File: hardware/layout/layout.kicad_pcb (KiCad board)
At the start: 4 copper layers, 50 x 20 mm, 73 parts, among them J1 208658-1001, J2 USB4105-GF-A-060, Q1 2N7002, SW1 TS-1088-AR02016, U1 PCA9306DCTR, U2 AP2112K-3.3TRG1, U3 USBLC6-2SC6, U4 W25Q16JVSSIQ, U5 RP2040, Y1 X322512MSB4SI

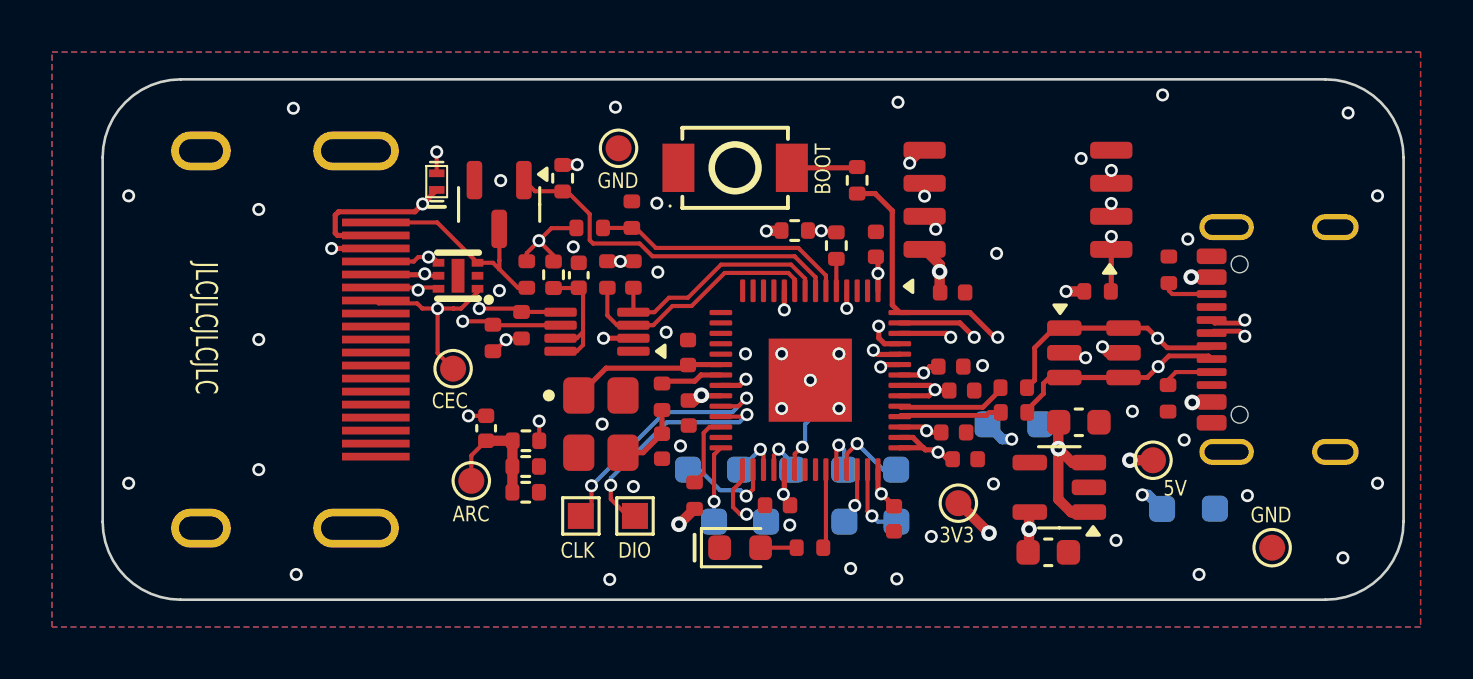
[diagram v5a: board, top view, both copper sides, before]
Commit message: hardware: adjust layout, add jlcpcb export to gitignore
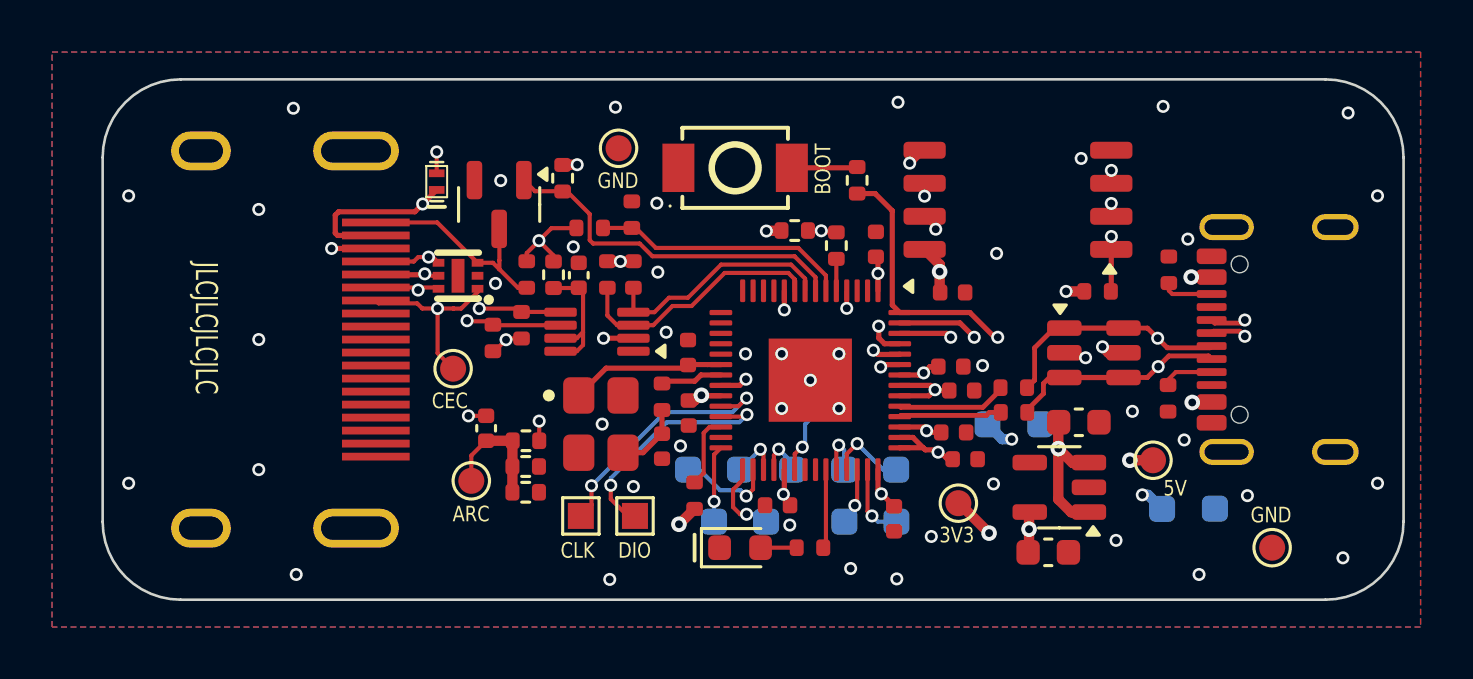
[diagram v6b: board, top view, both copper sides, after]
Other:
- board text added: "gh:naorunaoru/picoarc"
- board text removed: "@naorunaoru"
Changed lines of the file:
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@@
 		)
 	)
-	(gr_text "@naorunaoru"
+	(gr_text "gh:naorunaoru/picoarc"
 		(at 132.58 108.19 0)
 		(layer "B.SilkS")
 		(effects
 			(font
-				(size 1 1)
+				(size 0.8 0.8)
 				(thickness 0.1)
 			)
@@
 	)
 	(via
-		(at 115.25 109.12)
+		(at 115.099171 108.842136)
 		(size 0.5)
 		(drill 0.3)
@@
 	)
 	(via
-		(at 140.74 101.6)
+		(at 140.76 102.04)
 		(size 0.5)
 		(drill 0.3)
@@
 	)
 	(segment
-		(start 113.84 110.3)
+		(start 114.029579 110.3)
 		(end 114.87 110.3)
 		(width 0.16)
@@
 	)
 	(segment
+		(start 114.87 110.3)
+		(end 115 110.43)
+		(width 0.16)
+		(layer "F.Cu")
+		(net "DDC_SCL_5V")
+	)
+	(segment
 		(start 112.380736 108.474819)
 		(end 112.25367 108.474819)
@@
 	)
 	(segment
-		(start 114.87 110.3)
-		(end 115 110.43)
+		(start 114.006121 110.276542)
+		(end 114.029579 110.3)
 		(width 0.16)
 		(layer "F.Cu")
@@
 	)
 	(via
-		(at 113.84 110.3)
+		(at 114.006121 110.276542)
 		(size 0.5)
 		(drill 0.3)
@@
 	)
 	(segment
-		(start 113.84 110.3)
-		(end 113.84 110.08)
+		(start 112.380736 108.620737)
+		(end 112.380736 108.474819)
 		(width 0.16)
 		(layer "In1.Cu")
@@
 	)
 	(segment
-		(start 113.84 110.08)
-		(end 112.380736 108.620736)
+		(start 114.006121 110.246122)
+		(end 112.380736 108.620737)
 		(width 0.16)
 		(layer "In1.Cu")
@@
 	)
 	(segment
-		(start 112.380736 108.620736)
-		(end 112.380736 108.474819)
+		(start 114.006121 110.276542)
+		(end 114.006121 110.246122)
 		(width 0.16)
 		(layer "In1.Cu")
@@
 	)
 	(segment
-		(start 115.970001 109.810001)
-		(end 116.1 109.94)
+		(start 111.96 108)
+		(end 112.129363 107.830637)
 		(width 0.16)
 		(layer "F.Cu")
@@
 	)
 	(segment
-		(start 111.96 108)
-		(end 112.129363 107.830637)
+		(start 115.970001 109.810001)
+		(end 116.1 109.94)
 		(width 0.16)
 		(layer "F.Cu")
@@
 	)
 	(segment
-		(start 117.59 109.94)
-		(end 117.6 109.95)
+		(start 114.472964 109.810001)
+		(end 115.970001 109.810001)
 		(width 0.16)
 		(layer "F.Cu")
@@
 	)
 	(segment
-		(start 112.129363 107.830637)
-		(end 112.524381 107.830637)
+		(start 117.59 109.94)
+		(end 117.6 109.95)
 		(width 0.16)
 		(layer "F.Cu")
@@
 	)
 	(segment
-		(start 114.472964 109.810001)
-		(end 115.970001 109.810001)
+		(start 112.129363 107.830637)
+		(end 112.524381 107.830637)
 		(width 0.16)
 		(layer "F.Cu")
@@
 	(segment
 		(start 112.583701 107.984819)
-		(end 112.870736 108.271854)
+		(end 112.583701 107.889957)
 		(width 0.16)
 		(layer "In1.Cu")
@@
 	)
 	(segment
-		(start 112.524381 107.830637)
-		(end 112.583701 107.889957)
+		(start 114.472964 109.810001)
+		(end 114.180001 109.810001)
 		(width 0.16)
 		(layer "In1.Cu")
@@
 	)
 	(segment
-		(start 112.583701 107.889957)
-		(end 112.583701 107.984819)
+		(start 112.870736 108.500736)
+		(end 112.870736 108.271854)
 		(width 0.16)
 		(layer "In1.Cu")
@@
 	)
 	(segment
-		(start 114.180001 109.810001)
-		(end 114.472964 109.810001)
+		(start 112.583701 107.889957)
+		(end 112.524381 107.830637)
 		(width 0.16)
 		(layer "In1.Cu")
@@
 	)
 	(segment
-		(start 112.870736 108.500736)
-		(end 114.180001 109.810001)
+		(start 112.870736 108.271854)
+		(end 112.583701 107.984819)
 		(width 0.16)
 		(layer "In1.Cu")
@@
 	)
 	(segment
-		(start 112.870736 108.271854)
+		(start 114.180001 109.810001)
 		(end 112.870736 108.500736)
 		(width 0.16)
